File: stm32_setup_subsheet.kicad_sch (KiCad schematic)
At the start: 9 parts, among them J5 Programming Header, SW2 Reset Switch, U2 MAX7375AXR805

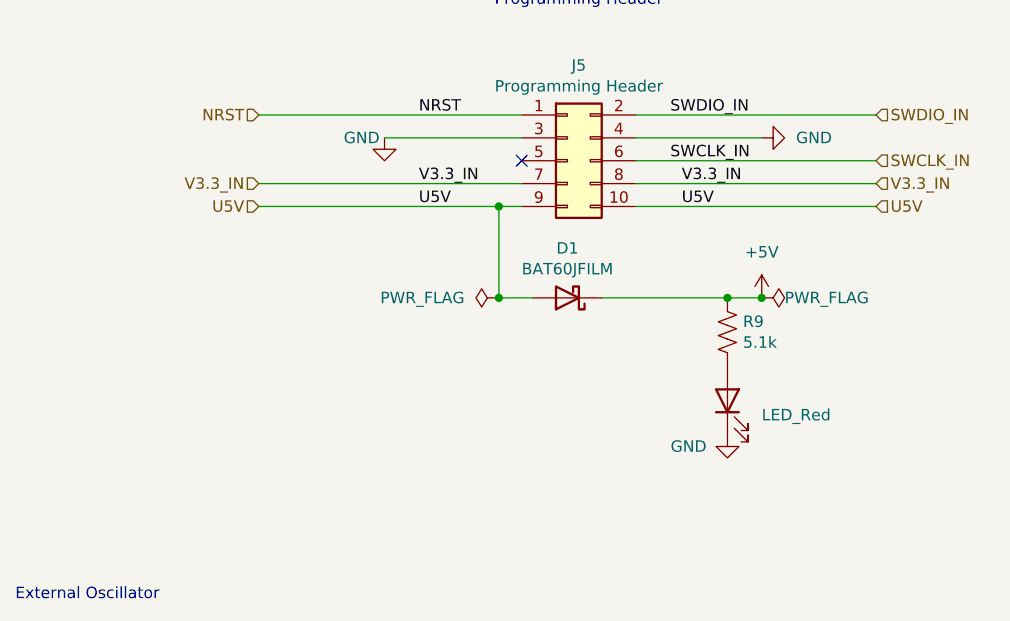
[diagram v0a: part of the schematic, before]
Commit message: remove un-needed program header circuitry, add debug LEDs, add USB ESD, add shcotty for LM117
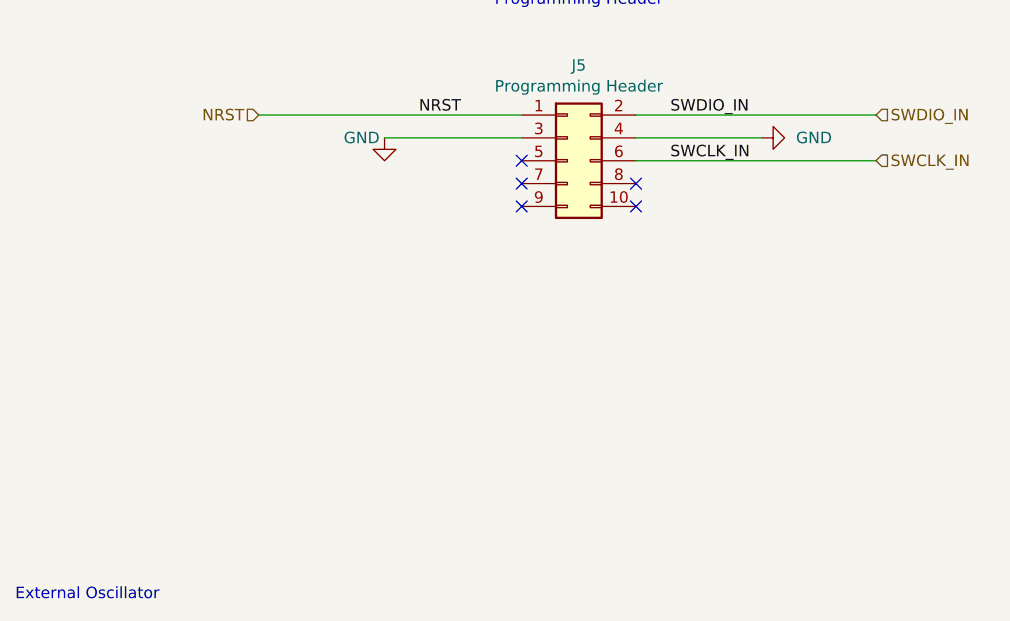
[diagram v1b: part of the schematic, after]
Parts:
- removed D1: BAT60JFILM, Diode_SMD:D_0805_2012Metric_Pad1.15x1.40mm_HandSolder, symbol Diode:BAT60A
- removed D7: LED_Red, LED_SMD:LED_0805_2012Metric_Pad1.15x1.40mm_HandSolder, symbol Device:LED
- removed R9: 5.1k, Resistor_SMD:R_0805_2012Metric_Pad1.20x1.40mm_HandSolder, symbol Device:R_US
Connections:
- net U5V: no longer names the net of J5.10 (Pin_10)
- net U5V: no longer J5.9 (Pin_9)
- net V3.3_IN: no longer names the net of J5.7 (Pin_7)
- net V3.3_IN: no longer J5.8 (Pin_8)
- no-connect marks 1 -> 5

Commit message: starter PCB
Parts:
- renumbered C2 to C14, C1 to C15, J5 to J2, R1 to R15, SW2 to SW1, U2 to U5
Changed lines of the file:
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@@
 		(on_board yes)
 		(dnp no)
-		(property "Reference" "#PWR014"
+		(property "Reference" "#PWR032"
 			(at 125.73 123.19 0)
 			(effects
@@
 			(project "PCB_Schematic"
 				(path "/a0c17764-e0d1-4df5-b871-1489cf266494/77009ed7-b9d0-4599-9e36-0d7b5cc2a84b"
-					(reference "#PWR014")
+					(reference "#PWR032")
 					(unit 1)
 				)
@@
 		(dnp no)
 		(fields_autoplaced yes)
-		(property "Reference" "U2"
+		(property "Reference" "U5"
 			(at 138.43 124.4599 0)
 			(effects
@@
 			(project "PCB_Schematic"
 				(path "/a0c17764-e0d1-4df5-b871-1489cf266494/77009ed7-b9d0-4599-9e36-0d7b5cc2a84b"
-					(reference "U2")
+					(reference "U5")
 					(unit 1)
 				)
@@
 		(on_board yes)
 		(dnp no)
-		(property "Reference" "J5"
+		(property "Reference" "J2"
 			(at 195.58 41.4782 0)
 			(effects
@@
 			(project "PCB_Schematic"
 				(path "/a0c17764-e0d1-4df5-b871-1489cf266494/77009ed7-b9d0-4599-9e36-0d7b5cc2a84b"
-					(reference "J5")
+					(reference "J2")
 					(unit 1)
 				)
@@
 		(dnp no)
 		(fields_autoplaced yes)
-		(property "Reference" "#PWR067"
+		(property "Reference" "#PWR034"
 			(at 144.78 140.97 0)
 			(effects
@@
 			(project "PCB_Schematic"
 				(path "/a0c17764-e0d1-4df5-b871-1489cf266494/77009ed7-b9d0-4599-9e36-0d7b5cc2a84b"
-					(reference "#PWR067")
+					(reference "#PWR034")
 					(unit 1)
 				)
@@
 		(on_board yes)
 		(dnp no)
-		(property "Reference" "C1"
+		(property "Reference" "C15"
 			(at 132.842 107.442 90)
 			(effects
@@
 			(project "PCB_Schematic"
 				(path "/a0c17764-e0d1-4df5-b871-1489cf266494/77009ed7-b9d0-4599-9e36-0d7b5cc2a84b"
-					(reference "C1")
+					(reference "C15")
 					(unit 1)
 				)
@@
 		(on_board yes)
 		(dnp no)
-		(property "Reference" "R1"
+		(property "Reference" "R15"
 			(at 84.2772 50.9016 0)
 			(effects
@@
 			(project "PCB_Schematic"
 				(path "/a0c17764-e0d1-4df5-b871-1489cf266494/77009ed7-b9d0-4599-9e36-0d7b5cc2a84b"
-					(reference "R1")
+					(reference "R15")
 					(unit 1)
 				)
@@
 		(on_board yes)
 		(dnp no)
-		(property "Reference" "#PWR021"
+		(property "Reference" "#PWR031"
 			(at 82.55 74.93 0)
 			(effects
@@
 			(project "PCB_Schematic"
 				(path "/a0c17764-e0d1-4df5-b871-1489cf266494/77009ed7-b9d0-4599-9e36-0d7b5cc2a84b"
-					(reference "#PWR021")
+					(reference "#PWR031")
 					(unit 1)
 				)
@@
 		(on_board yes)
 		(dnp no)
-		(property "Reference" "#PWR01"
+		(property "Reference" "#PWR035"
 			(at 173.99 55.88 0)
 			(effects
@@
 			(project "PCB_Schematic"
 				(path "/a0c17764-e0d1-4df5-b871-1489cf266494/77009ed7-b9d0-4599-9e36-0d7b5cc2a84b"
-					(reference "#PWR01")
+					(reference "#PWR035")
 					(unit 1)
 				)
@@
 		(on_board yes)
 		(dnp no)
-		(property "Reference" "C2"
+		(property "Reference" "C14"
 			(at 85.09 62.23 0)
 			(effects
@@
 			(project "PCB_Schematic"
 				(path "/a0c17764-e0d1-4df5-b871-1489cf266494/77009ed7-b9d0-4599-9e36-0d7b5cc2a84b"
-					(reference "C2")
+					(reference "C14")
 					(unit 1)
 				)
@@
 		(dnp no)
 		(fields_autoplaced yes)
-		(property "Reference" "#PWR020"
+		(property "Reference" "#PWR030"
 			(at 82.55 52.07 0)
 			(effects
@@
 			(project "PCB_Schematic"
 				(path "/a0c17764-e0d1-4df5-b871-1489cf266494/77009ed7-b9d0-4599-9e36-0d7b5cc2a84b"
-					(reference "#PWR020")
+					(reference "#PWR030")
 					(unit 1)
 				)
@@
 		(on_board yes)
 		(dnp no)
-		(property "Reference" "#PWR09"
+		(property "Reference" "#PWR029"
 			(at 69.85 62.23 0)
 			(effects
@@
 			(project "PCB_Schematic"
 				(path "/a0c17764-e0d1-4df5-b871-1489cf266494/77009ed7-b9d0-4599-9e36-0d7b5cc2a84b"
-					(reference "#PWR09")
+					(reference "#PWR029")
 					(unit 1)
 				)
@@
 		(dnp no)
 		(fields_autoplaced yes)
-		(property "Reference" "#PWR022"
+		(property "Reference" "#PWR033"
 			(at 144.78 114.3 0)
 			(effects
@@
 			(project "PCB_Schematic"
 				(path "/a0c17764-e0d1-4df5-b871-1489cf266494/77009ed7-b9d0-4599-9e36-0d7b5cc2a84b"
-					(reference "#PWR022")
+					(reference "#PWR033")
 					(unit 1)
 				)
@@
 		(dnp no)
 		(fields_autoplaced yes)
-		(property "Reference" "#PWR069"
+		(property "Reference" "#PWR036"
 			(at 222.25 49.53 0)
 			(effects
@@
 			(project "PCB_Schematic"
 				(path "/a0c17764-e0d1-4df5-b871-1489cf266494/77009ed7-b9d0-4599-9e36-0d7b5cc2a84b"
-					(reference "#PWR069")
+					(reference "#PWR036")
 					(unit 1)
 				)
@@
 		(dnp no)
 		(fields_autoplaced yes)
-		(property "Reference" "SW2"
+		(property "Reference" "SW1"
 			(at 74.93 48.26 0)
 			(effects
@@
 			(project "PCB_Schematic"
 				(path "/a0c17764-e0d1-4df5-b871-1489cf266494/77009ed7-b9d0-4599-9e36-0d7b5cc2a84b"
-					(reference "SW2")
-					(unit 1)
-				)
+					(reference "SW1")
+					(unit 1)
+				)

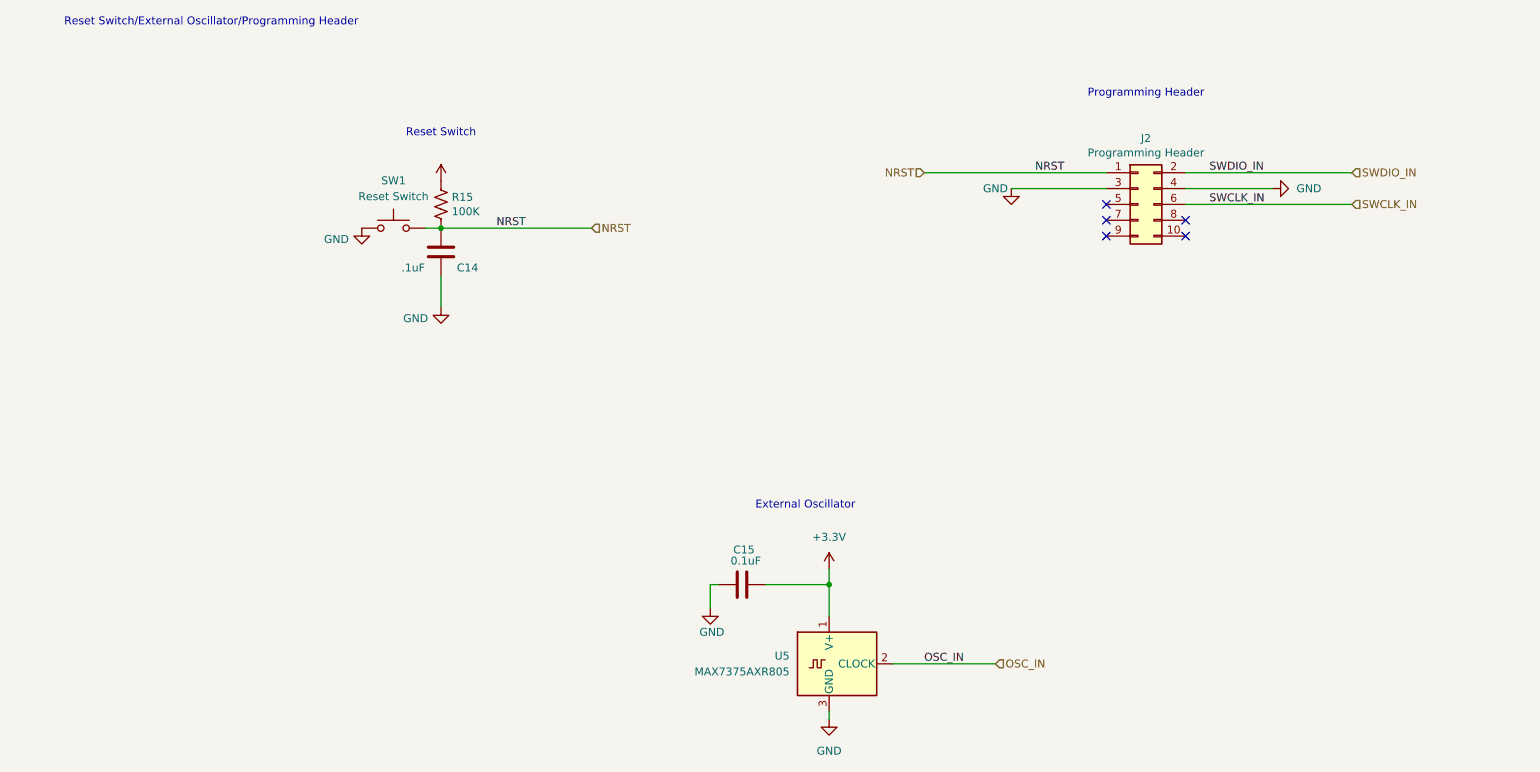
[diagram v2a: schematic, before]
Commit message: added testpoints to schematic for important sigs
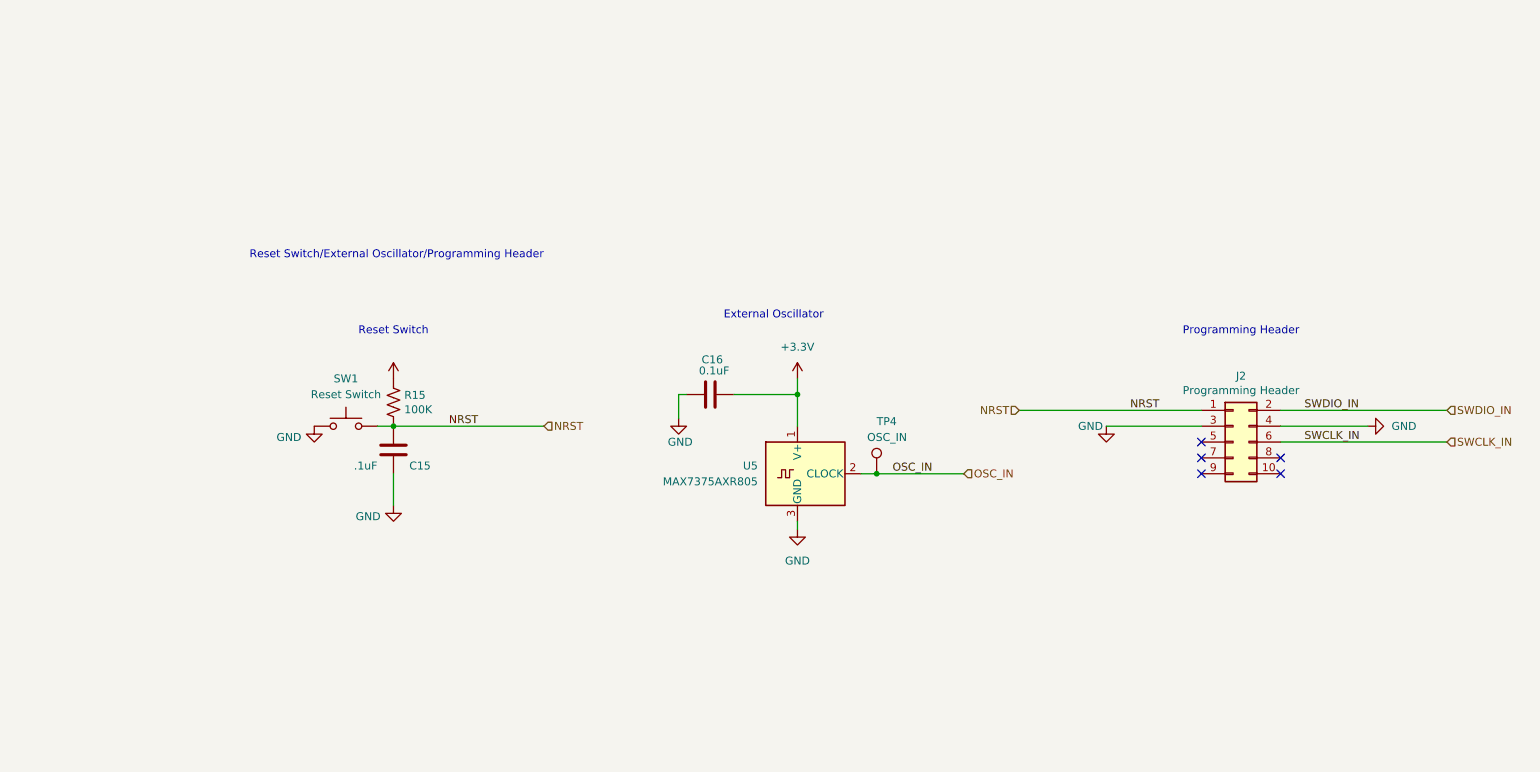
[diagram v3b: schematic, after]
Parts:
- added TP4: OSC_IN, symbol Connector:TestPoint
- renumbered C14 to C15, C15 to C16
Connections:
- net OSC_IN: now also TP4.1
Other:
- moved on the sheet: C15, C16, J2, R15, SW1, U5

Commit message: BOM done
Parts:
- SW1: footprint Button_Switch_SMD:SW_SPST_PTS645 -> Library:SW_TS04-66-55-BK-160-SMT
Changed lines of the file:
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@@
 			)
 		)
-		(property "Footprint" "Button_Switch_SMD:SW_SPST_PTS645"
+		(property "Footprint" "Library:SW_TS04-66-55-BK-160-SMT"
 			(at 67.31 82.55 0)
 			(effects

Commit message: footprint verf
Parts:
- renumbered TP4 to TP3
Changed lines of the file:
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@@
 		(on_board yes)
 		(dnp no)
-		(property "Reference" "#PWR032"
+		(property "Reference" "#PWR030"
 			(at 120.65 92.71 0)
 			(effects
@@
 			(project "PCB_Schematic"
 				(path "/a0c17764-e0d1-4df5-b871-1489cf266494/77009ed7-b9d0-4599-9e36-0d7b5cc2a84b"
-					(reference "#PWR032")
+					(reference "#PWR030")
 					(unit 1)
 				)
@@
 		(on_board yes)
 		(dnp no)
-		(property "Reference" "TP4"
+		(property "Reference" "TP3"
 			(at 152.4 86.868 0)
 			(effects
@@
 			(project ""
 				(path "/a0c17764-e0d1-4df5-b871-1489cf266494/77009ed7-b9d0-4599-9e36-0d7b5cc2a84b"
-					(reference "TP4")
+					(reference "TP3")
 					(unit 1)
 				)
@@
 		(dnp no)
 		(fields_autoplaced yes)
-		(property "Reference" "#PWR034"
+		(property "Reference" "#PWR032"
 			(at 139.7 110.49 0)
 			(effects
@@
 			(project "PCB_Schematic"
 				(path "/a0c17764-e0d1-4df5-b871-1489cf266494/77009ed7-b9d0-4599-9e36-0d7b5cc2a84b"
-					(reference "#PWR034")
+					(reference "#PWR032")
 					(unit 1)
 				)
@@
 		(on_board yes)
 		(dnp no)
-		(property "Reference" "#PWR031"
+		(property "Reference" "#PWR029"
 			(at 74.93 106.68 0)
 			(effects
@@
 			(project "PCB_Schematic"
 				(path "/a0c17764-e0d1-4df5-b871-1489cf266494/77009ed7-b9d0-4599-9e36-0d7b5cc2a84b"
-					(reference "#PWR031")
+					(reference "#PWR029")
 					(unit 1)
 				)
@@
 		(on_board yes)
 		(dnp no)
-		(property "Reference" "#PWR035"
+		(property "Reference" "#PWR033"
 			(at 189.23 93.98 0)
 			(effects
@@
 			(project "PCB_Schematic"
 				(path "/a0c17764-e0d1-4df5-b871-1489cf266494/77009ed7-b9d0-4599-9e36-0d7b5cc2a84b"
-					(reference "#PWR035")
+					(reference "#PWR033")
 					(unit 1)
 				)
@@
 		(dnp no)
 		(fields_autoplaced yes)
-		(property "Reference" "#PWR030"
+		(property "Reference" "#PWR028"
 			(at 74.93 83.82 0)
 			(effects
@@
 			(project "PCB_Schematic"
 				(path "/a0c17764-e0d1-4df5-b871-1489cf266494/77009ed7-b9d0-4599-9e36-0d7b5cc2a84b"
-					(reference "#PWR030")
+					(reference "#PWR028")
 					(unit 1)
 				)
@@
 		(on_board yes)
 		(dnp no)
-		(property "Reference" "#PWR029"
+		(property "Reference" "#PWR027"
 			(at 62.23 93.98 0)
 			(effects
@@
 			(project "PCB_Schematic"
 				(path "/a0c17764-e0d1-4df5-b871-1489cf266494/77009ed7-b9d0-4599-9e36-0d7b5cc2a84b"
-					(reference "#PWR029")
+					(reference "#PWR027")
 					(unit 1)
 				)
@@
 		(dnp no)
 		(fields_autoplaced yes)
-		(property "Reference" "#PWR033"
+		(property "Reference" "#PWR031"
 			(at 139.7 83.82 0)
 			(effects
@@
 			(project "PCB_Schematic"
 				(path "/a0c17764-e0d1-4df5-b871-1489cf266494/77009ed7-b9d0-4599-9e36-0d7b5cc2a84b"
-					(reference "#PWR033")
+					(reference "#PWR031")
 					(unit 1)
 				)
@@
 		(dnp no)
 		(fields_autoplaced yes)
-		(property "Reference" "#PWR036"
+		(property "Reference" "#PWR034"
 			(at 237.49 87.63 0)
 			(effects
@@
 			(project "PCB_Schematic"
 				(path "/a0c17764-e0d1-4df5-b871-1489cf266494/77009ed7-b9d0-4599-9e36-0d7b5cc2a84b"
-					(reference "#PWR036")
-					(unit 1)
-				)
+					(reference "#PWR034")
+					(unit 1)
+				)

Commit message: footprint
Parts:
- renumbered J2 to J1, R15 to R13
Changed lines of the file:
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@@
 		(on_board yes)
 		(dnp no)
-		(property "Reference" "J2"
+		(property "Reference" "J1"
 			(at 210.82 79.5782 0)
 			(effects
@@
 			(project "PCB_Schematic"
 				(path "/a0c17764-e0d1-4df5-b871-1489cf266494/77009ed7-b9d0-4599-9e36-0d7b5cc2a84b"
-					(reference "J2")
+					(reference "J1")
 					(unit 1)
 				)
@@
 		(on_board yes)
 		(dnp no)
-		(property "Reference" "R15"
+		(property "Reference" "R13"
 			(at 76.6572 82.6516 0)
 			(effects
@@
 			(project "PCB_Schematic"
 				(path "/a0c17764-e0d1-4df5-b871-1489cf266494/77009ed7-b9d0-4599-9e36-0d7b5cc2a84b"
-					(reference "R15")
-					(unit 1)
-				)
+					(reference "R13")
+					(unit 1)
+				)

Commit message: updates
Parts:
- removed TP3: OSC_IN, symbol Connector:TestPoint
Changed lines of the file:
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@@
 	(paper "A4")
-	(junction
-		(at 152.4 95.25)
-		(diameter 0)
-		(color 0 0 0 0)
-	)
 	(junction
 		(at 74.93 87.63)
@@
 	(wire
 		(pts
-			(xy 149.86 95.25) (xy 152.4 95.25)
-		)
-		(stroke
-			(width 0)
-			(type default)
-		)
-	)
-	(wire
-		(pts
-			(xy 152.4 95.25) (xy 166.37 95.25)
+			(xy 149.86 95.25) (xy 166.37 95.25)
 		)
 		(stroke
@@
 					(unit 1)
 				)
-			)
-		)
-	)
-	(symbol
-		(lib_id "Connector:TestPoint")
-		(at 152.4 95.25 0)
-		(unit 1)
-		(exclude_from_sim no)
-		(in_bom yes)
-		(on_board yes)
-		(dnp no)
-		(property "Reference" "TP3"
-			(at 152.4 86.868 0)
-			(effects
-				(font
-					(size 1.27 1.27)
-				)
-				(justify left)
-			)
-		)
-		(property "Value" "OSC_IN"
-			(at 150.876 89.408 0)
-			(effects
-				(font
-					(size 1.27 1.27)
-				)
-				(justify left)
-			)
-		)
-		(property "Footprint" ""
-			(at 157.48 95.25 0)
-			(effects
-				(font
-					(size 1.27 1.27)
-				)
-				(hide yes)
-			)
-		)
-		(property "Datasheet" "~"
-			(at 157.48 95.25 0)
-			(effects
-				(font
-					(size 1.27 1.27)
-				)
-				(hide yes)
-			)
-		)
-		(property "Description" "test point"
-			(at 152.4 95.25 0)
-			(effects
-				(font
-					(size 1.27 1.27)
-				)
-				(hide yes)
-			)
-		)
-		(pin "1"
-		)
-		(instances
-			(project ""
-				(path "/a0c17764-e0d1-4df5-b871-1489cf266494/77009ed7-b9d0-4599-9e36-0d7b5cc2a84b"
-					(reference "TP3")
-					(unit 1)
-				)
